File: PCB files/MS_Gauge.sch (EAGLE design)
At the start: 33 parts, among them IC1 B1836M, IC2 LPC11C24_QFP48, IC3 24LC32AT-I/OT, U1 MCP1700, U2 TSR1-2450, Y1 12MHz

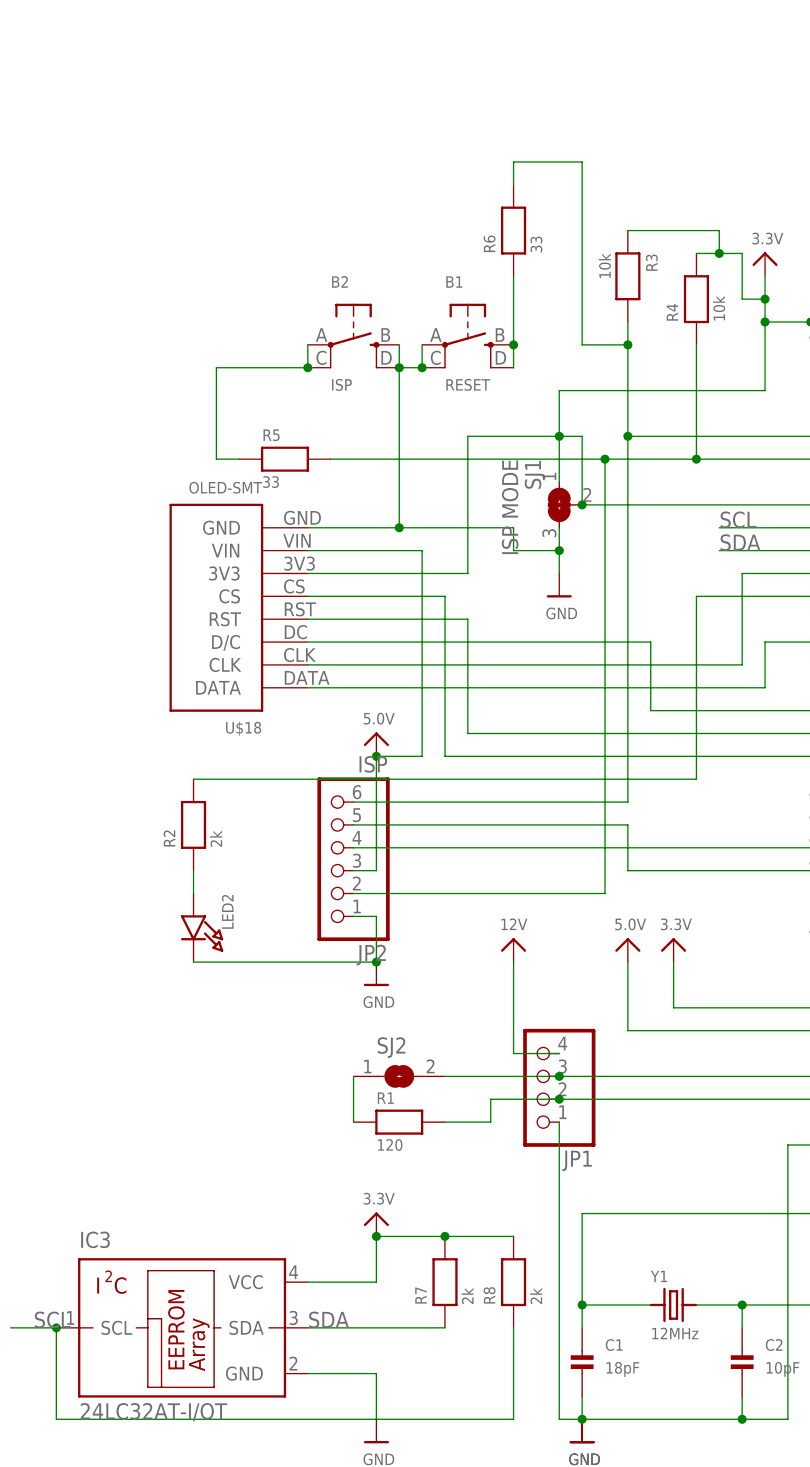
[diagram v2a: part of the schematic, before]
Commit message: Minor routing changes to PCB
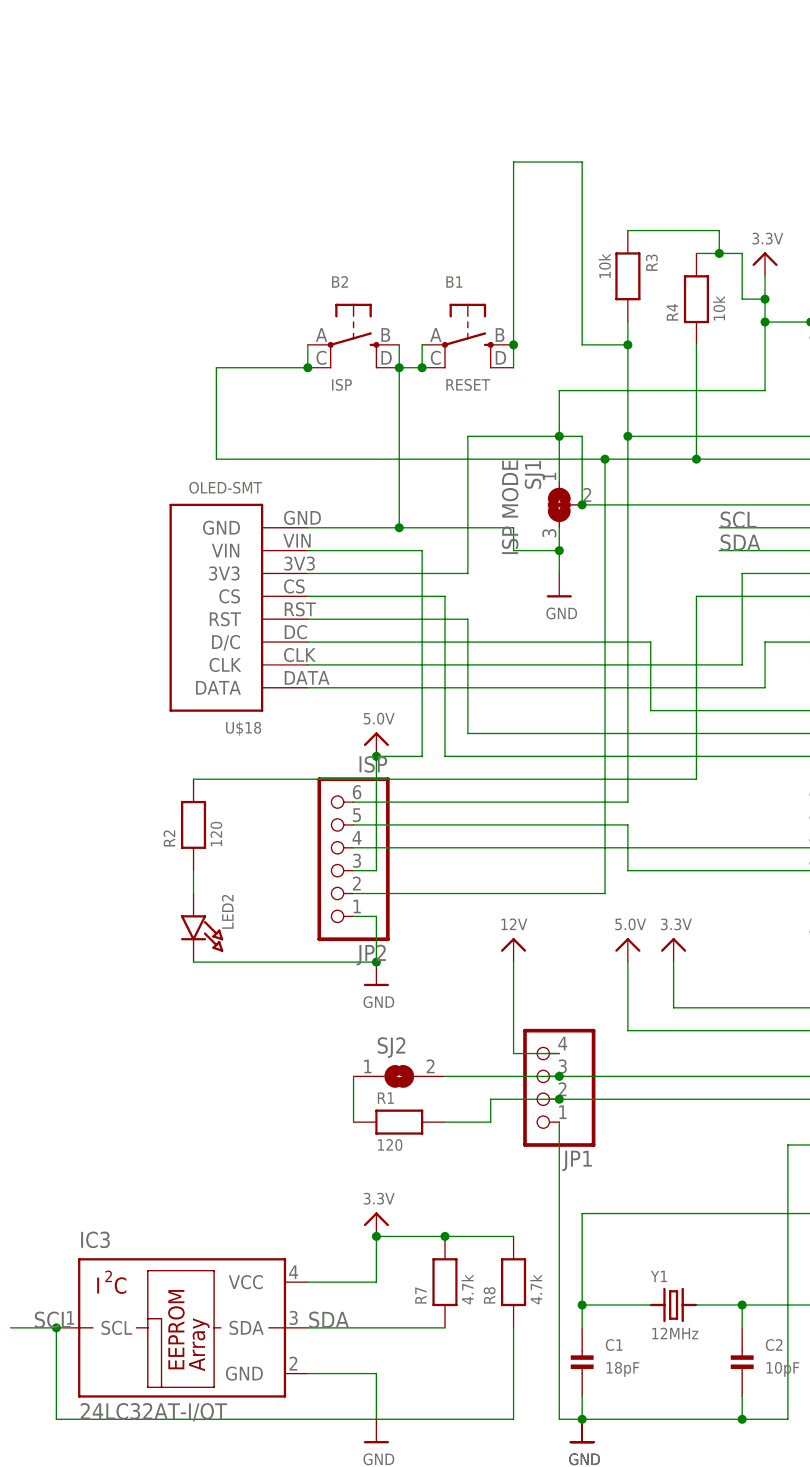
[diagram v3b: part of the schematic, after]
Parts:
- removed R5, R6: 33, microbuilder:RESISTOR0603
- R2: value 2k -> 120
- R7, R8: value 2k -> 4.7k
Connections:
- removed net N$13: IC2.RESET/PIO0_0, JP2.6, R3.2, R6.2
- removed net N$5: B2.P, B2.P1, R5.1
- net N$6: now also B2.P, B2.P1; no longer R5.2
- net N$8: now also IC2.RESET/PIO0_0, JP2.6, R3.2; no longer R6.1
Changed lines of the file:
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@@
 <part name="LOGO1" library="SparkFun-Aesthetics" deviceset="OSHW-LOGO" device="L"/>
 <part name="LED2" library="microbuilder" deviceset="LED" device="0603"/>
-<part name="R2" library="microbuilder" deviceset="RESISTOR" device="0603" value="2k"/>
+<part name="R2" library="microbuilder" deviceset="RESISTOR" device="0603" value="120"/>
 <part name="U1" library="microbuilder" deviceset="MCP1700" device=""/>
 <part name="U$1" library="Evans" deviceset="VID29-FLIPPED" device=""/>
@@
 <part name="U$2" library="microbuilder" deviceset="3.3V" device=""/>
 <part name="B2" library="microbuilder" deviceset="SWITCH_TACT_SMT" device="EVQPQ" value="ISP"/>
-<part name="R5" library="microbuilder" deviceset="RESISTOR" device="0603" value="33"/>
-<part name="R6" library="microbuilder" deviceset="RESISTOR" device="0603" value="33"/>
 <part name="SJ2" library="microbuilder" deviceset="SOLDERJUMPER" device=""/>
 <part name="U$21" library="microbuilder" deviceset="3.3V" device=""/>
 <part name="U$22" library="microbuilder" deviceset="GND" device=""/>
 <part name="U$23" library="microbuilder" deviceset="GND" device=""/>
-<part name="R7" library="microbuilder" deviceset="RESISTOR" device="0603" value="2k"/>
-<part name="R8" library="microbuilder" deviceset="RESISTOR" device="0603" value="2k"/>
+<part name="R7" library="microbuilder" deviceset="RESISTOR" device="0603" value="4.7k"/>
+<part name="R8" library="microbuilder" deviceset="RESISTOR" device="0603" value="4.7k"/>
 <part name="IC3" library="microchip" deviceset="24LC32AT-I/OT" device=""/>
 </parts>
@@
 <instance part="U$2" gate="G$1" x="93.98" y="20.32"/>
 <instance part="B2" gate="G$1" x="-76.2" y="104.14"/>
-<instance part="R5" gate="G$1" x="-83.82" y="91.44"/>
-<instance part="R6" gate="G$1" x="-58.42" y="116.84" rot="R90"/>
 <instance part="SJ2" gate="1" x="-71.12" y="22.86"/>
 <instance part="U$21" gate="G$1" x="-73.66" y="7.62"/>
@@
 </segment>
 </net>
-<net name="N$13" class="0">
-<segment>
-<pinref part="IC2" gate="G$1" pin="RESET/PIO0_0"/>
-<wire x1="-25.4" y1="93.98" x2="-45.72" y2="93.98" width="0.1524" layer="91"/>
-<wire x1="-45.72" y1="93.98" x2="-45.72" y2="53.34" width="0.1524" layer="91"/>
-<pinref part="JP2" gate="A" pin="6"/>
-<wire x1="-45.72" y1="53.34" x2="-76.2" y2="53.34" width="0.1524" layer="91"/>
-<wire x1="-45.72" y1="93.98" x2="-45.72" y2="104.14" width="0.1524" layer="91"/>
-<junction x="-45.72" y="93.98"/>
-<pinref part="R3" gate="G$1" pin="2"/>
-<pinref part="R6" gate="G$1" pin="2"/>
-<wire x1="-45.72" y1="104.14" x2="-45.72" y2="106.68" width="0.1524" layer="91"/>
-<wire x1="-58.42" y1="121.92" x2="-58.42" y2="124.46" width="0.1524" layer="91"/>
-<wire x1="-58.42" y1="124.46" x2="-50.8" y2="124.46" width="0.1524" layer="91"/>
-<wire x1="-50.8" y1="124.46" x2="-50.8" y2="104.14" width="0.1524" layer="91"/>
-<wire x1="-50.8" y1="104.14" x2="-45.72" y2="104.14" width="0.1524" layer="91"/>
-<junction x="-45.72" y="104.14"/>
-</segment>
-</net>
 <net name="N$23" class="0">
 <segment>
@@
 <wire x1="-38.1" y1="104.14" x2="-38.1" y2="91.44" width="0.1524" layer="91"/>
 <junction x="-38.1" y="91.44"/>
-<pinref part="R5" gate="G$1" pin="2"/>
-<wire x1="-78.74" y1="91.44" x2="-48.26" y2="91.44" width="0.1524" layer="91"/>
+<wire x1="-91.44" y1="91.44" x2="-48.26" y2="91.44" width="0.1524" layer="91"/>
 <junction x="-48.26" y="91.44"/>
-</segment>
-</net>
-<net name="N$5" class="0">
-<segment>
 <pinref part="B2" gate="G$1" pin="P"/>
 <pinref part="B2" gate="G$1" pin="P1"/>
 <wire x1="-81.28" y1="101.6" x2="-81.28" y2="104.14" width="0.1524" layer="91"/>
-<pinref part="R5" gate="G$1" pin="1"/>
-<wire x1="-88.9" y1="91.44" x2="-91.44" y2="91.44" width="0.1524" layer="91"/>
 <wire x1="-91.44" y1="91.44" x2="-91.44" y2="101.6" width="0.1524" layer="91"/>
 <wire x1="-91.44" y1="101.6" x2="-81.28" y2="101.6" width="0.1524" layer="91"/>
@@
 <pinref part="B1" gate="G$1" pin="S"/>
 <wire x1="-58.42" y1="104.14" x2="-58.42" y2="101.6" width="0.1524" layer="91"/>
-<pinref part="R6" gate="G$1" pin="1"/>
-<wire x1="-58.42" y1="104.14" x2="-58.42" y2="111.76" width="0.1524" layer="91"/>
 <junction x="-58.42" y="104.14"/>
-</segment>
-</net>
+<pinref part="IC2" gate="G$1" pin="RESET/PIO0_0"/>
+<wire x1="-25.4" y1="93.98" x2="-45.72" y2="93.98" width="0.1524" layer="91"/>
+<wire x1="-45.72" y1="93.98" x2="-45.72" y2="53.34" width="0.1524" layer="91"/>
+<pinref part="JP2" gate="A" pin="6"/>
+<wire x1="-45.72" y1="53.34" x2="-76.2" y2="53.34" width="0.1524" layer="91"/>
+<wire x1="-45.72" y1="93.98" x2="-45.72" y2="104.14" width="0.1524" layer="91"/>
+<junction x="-45.72" y="93.98"/>
+<pinref part="R3" gate="G$1" pin="2"/>
+<wire x1="-45.72" y1="104.14" x2="-45.72" y2="106.68" width="0.1524" layer="91"/>
+<wire x1="-58.42" y1="124.46" x2="-50.8" y2="124.46" width="0.1524" layer="91"/>
+<wire x1="-50.8" y1="124.46" x2="-50.8" y2="104.14" width="0.1524" layer="91"/>
+<wire x1="-50.8" y1="104.14" x2="-45.72" y2="104.14" width="0.1524" layer="91"/>
+<junction x="-45.72" y="104.14"/>
+<wire x1="-58.42" y1="104.14" x2="-58.42" y2="124.46" width="0.1524" layer="91"/>
+</segment>
+</net>
